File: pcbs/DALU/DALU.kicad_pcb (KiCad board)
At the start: 2 copper layers, 66 parts, among them J201 Conn_02x20_Odd_Even, U201 74HC245, U202 74HC245, U203 74HC245, U301 74HC138, U401 74HC86, U402 74HC86, U403 74HC86, U404 74HC283, U405 74HC283, U406 74HC245, U501 74HC00, U502 74HC00, U503 74HC14, U504 74HC14, U505 74HC245, U506 74HC245, U601 74HC86, U602 74HC86, U603 74HC245, U701 74HC245, U801 74HC74, U802 74HCT574

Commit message: Starting to do the routing. Schematic not yet complete, though
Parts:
- added D801: 1N4148, Diode_THT:D_DO-35_SOD27_P7.62mm_Horizontal, F.Cu at (254.0, 34.3)
- added D802: 1N4148, Diode_THT:D_DO-35_SOD27_P7.62mm_Horizontal, F.Cu at (254.0, 39.4)
- added D803: 1N4148, Diode_THT:D_DO-35_SOD27_P7.62mm_Horizontal, F.Cu at (254.0, 44.5)
- added R801: 100k, Resistor_THT:R_Axial_DIN0207_L6.3mm_D2.5mm_P7.62mm_Horizontal, F.Cu at (257.8, 47.0)
- added RN802: 10k, Resistor_SMD:R_Array_Convex_4x0402, F.Cu at (287.8, 22.6)
- added U404: 74HC08, Package_SO:SOIC-14_3.9x8.7mm_P1.27mm, F.Cu at (113.0, 92.7)
- added U408: 74HC245, Package_SO:SOIC-20W_7.5x12.8mm_P1.27mm, F.Cu at (118.1, 73.7)
- RN801: value R_Network08 -> 10k; footprint Resistor_THT:R_Array_SIP9 -> Resistor_SMD:R_Array_Convex_4x0402
- moved U402 66.6 mm to (74.9, 80.0)
- moved U405 44.5 mm to (96.5, 80.0)
- moved U502 36.1 mm to (109.2, 161.3)
- moved U504 36.1 mm to (129.5, 179.1)
- moved U506 36.1 mm to (141.0, 166.4)
- moved U501 36.1 mm to (109.2, 139.7)
- moved U505 36.1 mm to (139.7, 147.3)
- moved U503 36.1 mm to (129.5, 167.6)
- moved RN801 20.9 mm to (285.8, 8.89), turned to 0 degrees
- moved U407 9.92 mm to (118.1, 50.8)
- moved U202 3.81 mm to (58.4, 108.0)
- moved U401 3.81 mm to (74.9, 36.8)
- moved U403 3.81 mm to (74.9, 58.4)
- moved U406 2.03 mm to (96.5, 56.4)
- renumbered R801 to R802, U403 to U402, U402 to U403, U404 to U405, U405 to U406, U406 to U407
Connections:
- net /Output Stage/CLK renamed /Output Stage/EXECUTE
- RN801 pad 2: Net-(RN801-Pad2) -> GND
- RN801 pad 3: Net-(RN801-Pad3) -> GND
- RN801 pad 4: Net-(RN801-Pad4) -> GND
- RN801 pad 5: Net-(RN801-Pad5) -> Net-(U802-Pad5)
- RN801 pad 6: Net-(RN801-Pad6) -> Net-(U802-Pad4)
- RN801 pad 7: Net-(RN801-Pad7) -> Net-(U802-Pad3)
- RN801 pad 8: Net-(RN801-Pad8) -> Net-(U802-Pad2)
- U202 pad 1: unconnected-(U202-Pad1) -> +5V
- U202 pad 11: /Connector/A0 -> /AND-NAND/A0
- U202 pad 12: /Connector/A1 -> /AND-NAND/A1
- U202 pad 13: /Connector/A2 -> /AND-NAND/A2
- U202 pad 14: /Connector/A3 -> /AND-NAND/A3
- U202 pad 15: /Connector/A4 -> /AND-NAND/A4
- U202 pad 16: /Connector/A5 -> /AND-NAND/A5
- U202 pad 17: /Connector/A6 -> /AND-NAND/A6
- U202 pad 18: /Connector/A7 -> /AND-NAND/A7
- U203 pad 1: unconnected-(U203-Pad1) -> +5V
- U203 pad 11: /Connector/B0 -> /AND-NAND/B0
- U203 pad 12: /Connector/B1 -> /AND-NAND/B1
- U203 pad 13: /Connector/B2 -> /AND-NAND/B2
- U203 pad 14: /Connector/B3 -> /AND-NAND/B3
- U203 pad 15: /Connector/B4 -> /AND-NAND/B4
- U203 pad 16: /Connector/B5 -> /AND-NAND/B5
- U203 pad 17: /Connector/B6 -> /AND-NAND/B6
- U203 pad 18: /Connector/B7 -> /AND-NAND/B7
- U402 pad 1: Net-(U403-Pad1) -> /AdderSubtractor/~{ADD}
- U402 pad 10: (no net) -> /AdderSubtractor/~{ADD}
- U402 pad 11: /AdderSubtractor/~{ADD}/SUBTRACT -> unconnected-(U402-Pad11)
- U402 pad 12: GND -> unconnected-(U402-Pad12)
- U402 pad 13: Net-(U403-Pad13) -> unconnected-(U402-Pad13)
- U402 pad 2: /AdderSubtractor/~{ADD}/SUBTRACT -> GND
- U402 pad 3: unconnected-(U403-Pad3) -> Net-(U401-Pad10)
- U402 pad 4: Net-(U403-Pad13) -> /AdderSubtractor/~{ADD}
- U402 pad 5: unconnected-(U403-Pad5) -> GND
- U402 pad 6: unconnected-(U403-Pad6) -> Net-(U403-Pad10)
- U402 pad 8: (no net) -> Net-(U402-Pad8)
- U402 pad 9: (no net) -> Net-(U402-Pad9)
- U403 pad 10: Net-(U402-Pad10) -> Net-(U403-Pad10)
- U403 pad 13: Net-(U402-Pad10) -> Net-(U403-Pad10)
- U403 pad 2: Net-(U402-Pad10) -> Net-(U403-Pad10)
- U403 pad 5: Net-(U402-Pad10) -> Net-(U403-Pad10)
- U405 pad 7: /AdderSubtractor/~{ADD}/SUBTRACT -> /AdderSubtractor/~{ADD}
- U406 pad 9: Net-(U403-Pad1) -> Net-(U402-Pad9)
- U407 pad 1: /AdderSubtractor/~{ENABLE_{AS}} -> +5V
- U407 pad 19: /AdderSubtractor/~{ENABLE_{AS}} -> /AdderSubtractor/~{OE}
- U603 pad 1: unconnected-(U603-Pad1) -> +5V
- U701 pad 1: unconnected-(U701-Pad1) -> +5V
- U701 pad 19: unconnected-(U701-Pad19) -> /OR/~{OR}
- U802 pad 1: unconnected-(U802-Pad1) -> /Output Stage/~{OE}
- U802 pad 2: Net-(RN801-Pad9) -> Net-(U802-Pad2)
- U802 pad 3: Net-(RN801-Pad8) -> Net-(U802-Pad3)
- U802 pad 4: Net-(RN801-Pad7) -> Net-(U802-Pad4)
- U802 pad 5: Net-(RN801-Pad6) -> Net-(U802-Pad5)
- U802 pad 6: Net-(RN801-Pad5) -> Net-(U802-Pad6)
- U802 pad 7: Net-(RN801-Pad4) -> Net-(U802-Pad7)
- U802 pad 8: Net-(RN801-Pad3) -> Net-(U802-Pad8)
- U802 pad 9: Net-(RN801-Pad2) -> Net-(U802-Pad9)
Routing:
- net /AND-NAND/B1: track 0.00 -> 95.5 mm, vias 0 -> 1
- net /AND-NAND/B3: track 0.00 -> 89.1 mm, vias 0 -> 1
- net /AND-NAND/B2: track 0.00 -> 89.1 mm, vias 0 -> 1
- net /AND-NAND/B4: track 0.00 -> 87.1 mm, vias 0 -> 1
- net /AND-NAND/B5: track 0.00 -> 83.8 mm, vias 0 -> 1
- net /AND-NAND/B6: track 0.00 -> 78.2 mm, vias 0 -> 1
- net /AND-NAND/B7: track 0.00 -> 74.9 mm, vias 0 -> 1
- net /AND-NAND/A0: track 0.00 -> 66.1 mm, vias 0 -> 1
- net /AND-NAND/A2: track 0.00 -> 65.3 mm, vias 0 -> 1
- net /AND-NAND/B0: track 0.00 -> 64.7 mm, vias 0 -> 1
- net /AND-NAND/A5: track 0.00 -> 64.0 mm, vias 0 -> 1
- net /AND-NAND/A3: track 0.00 -> 64.0 mm, vias 0 -> 1
- net /AND-NAND/A4: track 0.00 -> 60.4 mm, vias 0 -> 1
- net /AND-NAND/A1: track 0.00 -> 59.7 mm, vias 0 -> 1
- net /AND-NAND/A6: track 0.00 -> 50.3 mm, vias 0 -> 1
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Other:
- copper layers 2 -> 4

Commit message: Fiddling with the adders
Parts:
- moved U401 39.7 mm to (72.4, 76.5)
- moved U402 34.1 mm to (41.1, 75.2)
- moved U406 13.3 mm to (85.1, 49.5)
- moved U405 12.4 mm to (85.1, 75.2)
- moved U403 8.04 mm to (72.4, 50.8)
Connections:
- net Net-(U405-Pad1) renamed /AdderSubtractor/S_{1}
- net Net-(U405-Pad10) renamed /AdderSubtractor/S_{3}
- net Net-(U405-Pad13) renamed /AdderSubtractor/S_{2}
- net Net-(U405-Pad4) renamed /AdderSubtractor/S_{0}
- net Net-(U406-Pad1) renamed /AdderSubtractor/S_{5}
- net Net-(U406-Pad10) renamed /AdderSubtractor/S_{7}
- net Net-(U406-Pad13) renamed /AdderSubtractor/S_{6}
- net Net-(U406-Pad4) renamed /AdderSubtractor/S_{4}
- U401 pad 1: /AND-NAND/B0 -> /AND-NAND/B2
- U401 pad 11: /AdderSubtractor/B'3 -> /AdderSubtractor/B'1
- U401 pad 12: /AND-NAND/B3 -> /AND-NAND/B1
- U401 pad 3: /AdderSubtractor/B'0 -> /AdderSubtractor/B'2
- U401 pad 4: /AND-NAND/B1 -> /AND-NAND/B3
- U401 pad 6: /AdderSubtractor/B'1 -> /AdderSubtractor/B'3
- U401 pad 8: /AdderSubtractor/B'2 -> /AdderSubtractor/B'0
- U401 pad 9: /AND-NAND/B2 -> /AND-NAND/B0
- U403 pad 1: /AND-NAND/B4 -> /AND-NAND/B6
- U403 pad 11: /AdderSubtractor/B'7 -> /AdderSubtractor/B'5
- U403 pad 12: /AND-NAND/B7 -> /AND-NAND/B5
- U403 pad 3: /AdderSubtractor/B'4 -> /AdderSubtractor/B'6
- U403 pad 4: /AND-NAND/B5 -> /AND-NAND/B7
- U403 pad 6: /AdderSubtractor/B'5 -> /AdderSubtractor/B'7
- U403 pad 8: /AdderSubtractor/B'6 -> /AdderSubtractor/B'4
- U403 pad 9: /AND-NAND/B6 -> /AND-NAND/B4
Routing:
- net /AdderSubtractor/B'6: track 0.00 -> 54.5 mm
- net /AdderSubtractor/B'2: track 0.00 -> 54.5 mm
- net /AdderSubtractor/B'1: track 0.00 -> 42.8 mm
- net /AdderSubtractor/B'5: track 0.00 -> 42.8 mm
- net /AND-NAND/A5: track 64.0 -> 102.2 mm
- net /AdderSubtractor/B'7: track 0.00 -> 37.8 mm
- net /AdderSubtractor/B'3: track 0.00 -> 37.8 mm
- net /AND-NAND/A6: track 50.3 -> 85.9 mm
- net /AND-NAND/A7: track 49.0 -> 82.6 mm
- net /AND-NAND/A4: track 60.4 -> 90.5 mm
- net /AND-NAND/B6: track 78.2 -> 104.5 mm
- net /AdderSubtractor/B'0: track 0.00 -> 22.0 mm
- net /AdderSubtractor/B'4: track 0.00 -> 22.0 mm
- net /AND-NAND/B7: track 74.9 -> 94.1 mm
- net /AND-NAND/B0: track 64.7 -> 46.8 mm
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
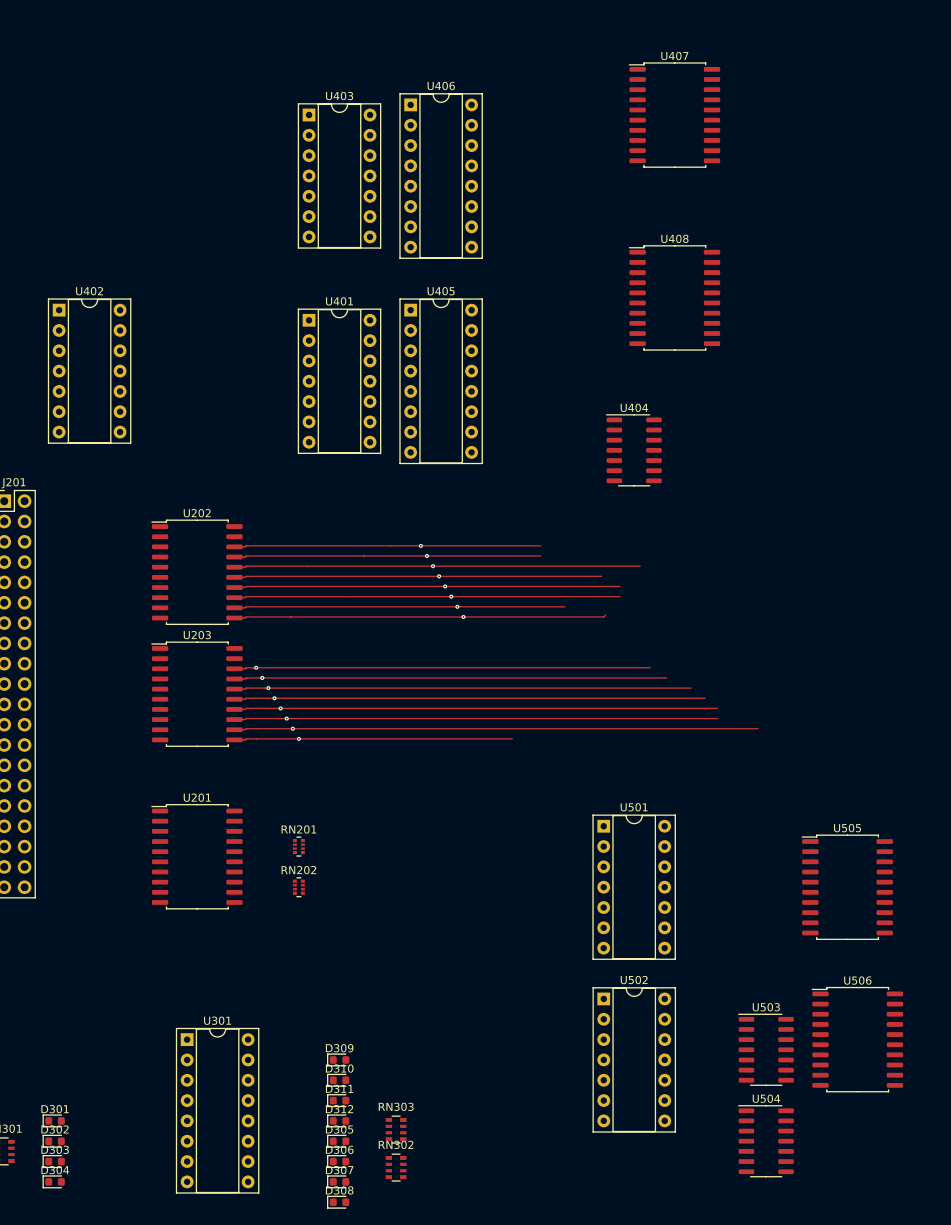
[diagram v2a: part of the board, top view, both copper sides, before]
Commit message: Rerouting
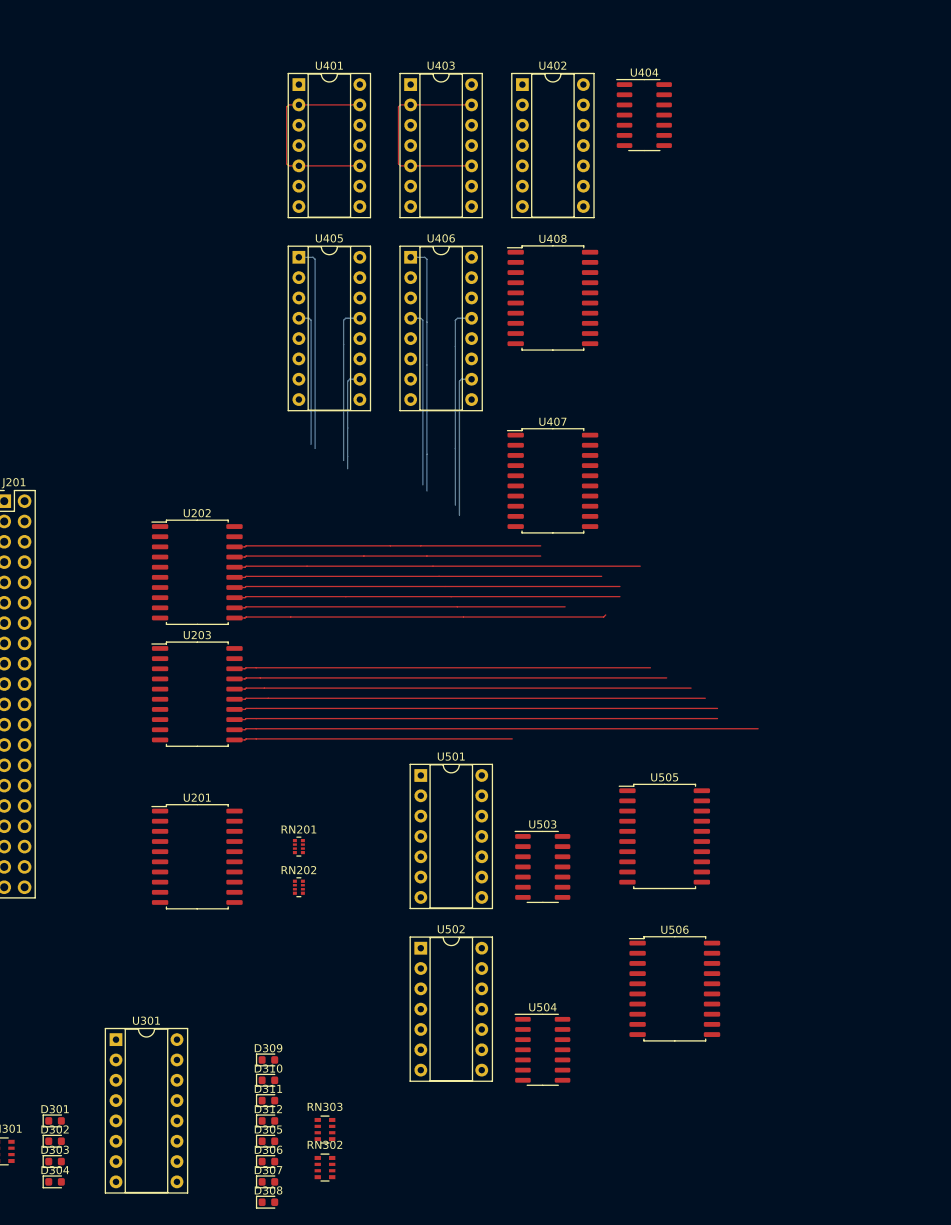
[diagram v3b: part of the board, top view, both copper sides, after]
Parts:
- moved U402 64.4 mm to (99.1, 47.0)
- moved U407 48.2 mm to (102.9, 96.5)
- moved U404 41.9 mm to (114.3, 50.8)
- moved U503 36.1 mm to (101.6, 144.8)
- moved U504 30.2 mm to (101.6, 167.6)
- moved U401 29.5 mm to (71.1, 47.0)
- moved U502 23.7 mm to (86.4, 154.9)
- moved U506 23.7 mm to (118.1, 160.0)
- moved U505 23.7 mm to (116.8, 141.0)
- moved U501 23.7 mm to (86.4, 133.3)
- moved U406 19.0 mm to (85.1, 68.6)
- moved U405 15.5 mm to (71.1, 68.6)
- moved U408 15.2 mm to (102.9, 73.7)
- moved U403 13.3 mm to (85.1, 47.0)
- moved D305 8.89 mm to (67.3, 179.1)
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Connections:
- net Net-(U503-Pad2) renamed /AND-NAND/AND0
- net Net-(U504-Pad2) renamed /AND-NAND/AND4
- net Net-(U504-Pad4) renamed /AND-NAND/AND5
- J201 pad 18: /Connector/A^{raw}_{0} -> Net-(J201-Pad18)
- J201 pad 23: /Connector/I^{raw}_{3} -> /Connector/I^{raw}_{0}
- J201 pad 24: Net-(J201-Pad24) -> /Connector/B^{raw}_{0}
- J201 pad 25: /Connector/I^{raw}_{2} -> /Connector/I^{raw}_{1}
- J201 pad 27: /Connector/I^{raw}_{1} -> /Connector/I^{raw}_{2}
- J201 pad 29: /Connector/I^{raw}_{0} -> /Connector/I^{raw}_{3}
- J201 pad 38: /Connector/B^{raw}_{0} -> Net-(J201-Pad38)
- J201 pad 4: Net-(J201-Pad4) -> /Connector/A^{raw}_{0}
- U201 pad 15: /Connector/Control.I0 -> /Connector/Control.I3
- U201 pad 16: /Connector/Control.I1 -> /Connector/Control.I2
- U201 pad 17: /Connector/Control.I2 -> /Connector/Control.I1
- U201 pad 18: /Connector/Control.I3 -> /Connector/Control.I0
- U201 pad 2: /Connector/I^{raw}_{3} -> /Connector/I^{raw}_{0}
- U201 pad 3: /Connector/I^{raw}_{2} -> /Connector/I^{raw}_{1}
- U201 pad 4: /Connector/I^{raw}_{1} -> /Connector/I^{raw}_{2}
- U201 pad 5: /Connector/I^{raw}_{0} -> /Connector/I^{raw}_{3}
- U202 pad 11: /AND-NAND/A0 -> /AND-NAND/A7
- U202 pad 12: /AND-NAND/A1 -> /AND-NAND/A6
- U202 pad 13: /AND-NAND/A2 -> /AND-NAND/A5
- U202 pad 14: /AND-NAND/A3 -> /AND-NAND/A4
- U202 pad 15: /AND-NAND/A4 -> /AND-NAND/A3
- U202 pad 16: /AND-NAND/A5 -> /AND-NAND/A2
- U202 pad 17: /AND-NAND/A6 -> /AND-NAND/A1
- U202 pad 18: /AND-NAND/A7 -> /AND-NAND/A0
- U202 pad 2: Net-(J201-Pad4) -> /Connector/A^{raw}_{0}
- U202 pad 9: /Connector/A^{raw}_{0} -> Net-(J201-Pad18)
- U203 pad 11: /AND-NAND/B0 -> /AND-NAND/B7
- U203 pad 12: /AND-NAND/B1 -> /AND-NAND/B6
- U203 pad 13: /AND-NAND/B2 -> /AND-NAND/B5
- U203 pad 14: /AND-NAND/B3 -> /AND-NAND/B4
- U203 pad 15: /AND-NAND/B4 -> /AND-NAND/B3
- U203 pad 16: /AND-NAND/B5 -> /AND-NAND/B2
- U203 pad 17: /AND-NAND/B6 -> /AND-NAND/B1
- U203 pad 18: /AND-NAND/B7 -> /AND-NAND/B0
- U203 pad 2: Net-(J201-Pad24) -> /Connector/B^{raw}_{0}
- U203 pad 9: /Connector/B^{raw}_{0} -> Net-(J201-Pad38)
- U401 pad 1: /AND-NAND/B2 -> /AND-NAND/B0
- U401 pad 11: /AdderSubtractor/B'1 -> /AdderSubtractor/B'3
- U401 pad 12: /AND-NAND/B1 -> /AND-NAND/B3
- U401 pad 3: /AdderSubtractor/B'2 -> /AdderSubtractor/B'0
- U401 pad 4: /AND-NAND/B3 -> /AND-NAND/B1
- U401 pad 6: /AdderSubtractor/B'3 -> /AdderSubtractor/B'1
- U401 pad 8: /AdderSubtractor/B'0 -> /AdderSubtractor/B'2
- U401 pad 9: /AND-NAND/B0 -> /AND-NAND/B2
- U403 pad 1: /AND-NAND/B6 -> /AND-NAND/B4
- U403 pad 11: /AdderSubtractor/B'5 -> /AdderSubtractor/B'7
- U403 pad 12: /AND-NAND/B5 -> /AND-NAND/B7
- U403 pad 3: /AdderSubtractor/B'6 -> /AdderSubtractor/B'4
- U403 pad 4: /AND-NAND/B7 -> /AND-NAND/B5
- U403 pad 6: /AdderSubtractor/B'7 -> /AdderSubtractor/B'5
- U403 pad 8: /AdderSubtractor/B'4 -> /AdderSubtractor/B'6
- U403 pad 9: /AND-NAND/B4 -> /AND-NAND/B6
- U503 pad 12: unconnected-(U503-Pad12) -> /AND-NAND/AND3
- U503 pad 13: unconnected-(U503-Pad13) -> /AND-NAND/NAND3
- U503 pad 3: /AND-NAND/NAND1 -> unconnected-(U503-Pad3)
- U503 pad 4: Net-(U503-Pad4) -> unconnected-(U503-Pad4)
- U503 pad 5: /AND-NAND/NAND6 -> /AND-NAND/NAND1
- U503 pad 6: Net-(U503-Pad6) -> /AND-NAND/AND1
- U503 pad 8: Net-(U503-Pad8) -> /AND-NAND/AND2
- U503 pad 9: /AND-NAND/NAND7 -> /AND-NAND/NAND2
- U504 pad 5: /AND-NAND/NAND2 -> /AND-NAND/NAND6
- U504 pad 6: Net-(U504-Pad6) -> /AND-NAND/AND6
- U504 pad 8: Net-(U504-Pad8) -> /AND-NAND/AND7
- U504 pad 9: /AND-NAND/NAND3 -> /AND-NAND/NAND7
- U505 pad 1: unconnected-(U505-Pad1) -> +5V
- U505 pad 11: unconnected-(U505-Pad11) -> /AND-NAND/RESULT7
- U505 pad 12: unconnected-(U505-Pad12) -> /AND-NAND/RESULT6
- U505 pad 13: unconnected-(U505-Pad13) -> /AND-NAND/RESULT5
- U505 pad 14: unconnected-(U505-Pad14) -> /AND-NAND/RESULT4
- U505 pad 15: unconnected-(U505-Pad15) -> /AND-NAND/RESULT3
- U505 pad 16: unconnected-(U505-Pad16) -> /AND-NAND/RESULT2
- U505 pad 17: unconnected-(U505-Pad17) -> /AND-NAND/RESULT1
- U505 pad 18: unconnected-(U505-Pad18) -> /AND-NAND/RESULT0
- U505 pad 19: unconnected-(U505-Pad19) -> /AND-NAND/~{NAND}
- U506 pad 1: unconnected-(U506-Pad1) -> +5V
- U506 pad 11: unconnected-(U506-Pad11) -> /AND-NAND/RESULT7
- U506 pad 12: unconnected-(U506-Pad12) -> /AND-NAND/RESULT6
- U506 pad 13: unconnected-(U506-Pad13) -> /AND-NAND/RESULT5
- U506 pad 14: unconnected-(U506-Pad14) -> /AND-NAND/RESULT4
- U506 pad 15: unconnected-(U506-Pad15) -> /AND-NAND/RESULT3
- U506 pad 16: unconnected-(U506-Pad16) -> /AND-NAND/RESULT2
- U506 pad 17: unconnected-(U506-Pad17) -> /AND-NAND/RESULT1
- U506 pad 18: unconnected-(U506-Pad18) -> /AND-NAND/RESULT0
- U506 pad 19: unconnected-(U506-Pad19) -> /AND-NAND/~{AND}
- U506 pad 3: Net-(U503-Pad4) -> /AND-NAND/AND1
- U506 pad 4: Net-(U504-Pad6) -> /AND-NAND/AND2
- U506 pad 5: Net-(U504-Pad8) -> /AND-NAND/AND3
- U506 pad 8: Net-(U503-Pad6) -> /AND-NAND/AND6
- U506 pad 9: Net-(U503-Pad8) -> /AND-NAND/AND7
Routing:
- net /AND-NAND/B0: track 46.8 -> 106.1 mm, vias 1 -> 0
- net /AdderSubtractor/B'6: track 54.5 -> 11.1 mm
- net /AdderSubtractor/B'2: track 54.5 -> 11.1 mm
- net /AND-NAND/B4: track 96.1 -> 137.1 mm, vias 1 -> 0
- net /AND-NAND/B3: track 75.8 -> 116.0 mm, vias 1 -> 0
- net /AND-NAND/B5: track 99.1 -> 137.3 mm, vias 1 -> 0
- net /AdderSubtractor/S_{5}: track 0.00 -> 31.1 mm
- net /AdderSubtractor/B'1: track 42.8 -> 13.7 mm
- net /AdderSubtractor/B'5: track 42.8 -> 13.7 mm
- net /AdderSubtractor/S_{1}: track 0.00 -> 25.8 mm
- net Net-(U402-Pad6): track 0.00 -> 25.6 mm
- net Net-(U401-Pad13): track 0.00 -> 25.6 mm
- net /AdderSubtractor/S_{6}: track 0.00 -> 25.3 mm
- net /AND-NAND/B6: track 104.5 -> 129.0 mm, vias 1 -> 0
- net /AdderSubtractor/S_{4}: track 0.00 -> 22.2 mm
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
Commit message: More routing
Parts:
- moved D701 57.4 mm to (133.3, 146.1), turned to 90 degrees
- moved R701 55.3 mm to (141.0, 146.1), turned to 90 degrees
- moved D702 52.1 mm to (137.2, 146.1), turned to 90 degrees
- moved D703 46.0 mm to (144.8, 147.3), turned to 90 degrees
- moved U701 45.3 mm to (186.7, 151.1)
- moved R702 44.4 mm to (152.4, 147.3), turned to 90 degrees
- moved D709 43.3 mm to (133.3, 157.5), turned to 90 degrees
- moved D704 40.9 mm to (148.6, 147.3), turned to 90 degrees
- moved R705 40.4 mm to (141.0, 157.5), turned to 90 degrees
- moved D710 37.9 mm to (137.2, 157.5), turned to 90 degrees
- moved D705 35.8 mm to (156.2, 148.6), turned to 90 degrees
- moved R703 34.9 mm to (163.8, 148.6), turned to 90 degrees
- moved D706 31.1 mm to (160.0, 148.6), turned to 90 degrees
- moved D711 30.5 mm to (144.8, 158.8), turned to 90 degrees
- moved R704 28.4 mm to (175.4, 149.9), turned to 90 degrees
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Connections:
- U501 pad 10: /AND-NAND/B3 -> /AND-NAND/B2
- U501 pad 11: /AND-NAND/NAND2 -> /AND-NAND/NAND3
- U501 pad 12: /AND-NAND/A2 -> /AND-NAND/A3
- U501 pad 13: /AND-NAND/B2 -> /AND-NAND/B3
- U501 pad 8: /AND-NAND/NAND3 -> /AND-NAND/NAND2
- U501 pad 9: /AND-NAND/A3 -> /AND-NAND/A2
- U502 pad 10: /AND-NAND/B7 -> /AND-NAND/B6
- U502 pad 11: /AND-NAND/NAND6 -> /AND-NAND/NAND7
- U502 pad 12: /AND-NAND/A6 -> /AND-NAND/A7
- U502 pad 13: /AND-NAND/B6 -> /AND-NAND/B7
- U502 pad 8: /AND-NAND/NAND7 -> /AND-NAND/NAND6
- U502 pad 9: /AND-NAND/A7 -> /AND-NAND/A6
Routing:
- net /AND-NAND/NAND1: track 0.00 -> 63.9 mm, vias 0 -> 2
- net /AND-NAND/NAND2: track 0.00 -> 62.1 mm, vias 0 -> 2
- net /AND-NAND/NAND5: track 0.00 -> 61.8 mm, vias 0 -> 2
- net /AND-NAND/NAND6: track 0.00 -> 61.6 mm, vias 0 -> 2
- net Net-(D709-Pad1): track 0.00 -> 54.0 mm
- net /AND-NAND/NAND4: track 0.00 -> 52.9 mm, vias 0 -> 2
- net /AND-NAND/NAND7: track 0.00 -> 51.4 mm, vias 0 -> 2
- net /AND-NAND/NAND0: track 0.00 -> 50.9 mm, vias 0 -> 2
- net Net-(D701-Pad1): track 0.00 -> 49.0 mm
- net /AND-NAND/NAND3: track 0.00 -> 46.6 mm, vias 0 -> 2
- net /AND-NAND/B7: track 114.2 -> 157.3 mm
- net Net-(D711-Pad1): track 0.00 -> 42.6 mm
- net Net-(D703-Pad1): track 0.00 -> 37.5 mm
- net /AND-NAND/A6: track 91.9 -> 126.5 mm
- net /AND-NAND/RESULT2: track 0.00 -> 33.8 mm, vias 0 -> 3
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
